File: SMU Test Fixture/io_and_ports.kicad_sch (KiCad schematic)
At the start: 45 parts, among them J1 AD2 Connector, J10 Ext. Source, J11 Conn_01x03, J12 105-1102-001, J2 Scope -1, J3 Scope +1, J4 Scope -2, J5 Scope +2, J6 WG1, J7 WG2, J8 AD2 Connector, J9 105-1102-001, U10 ADGS1412, U11 ADGS1412, U16 OPA189IDBVx, U17 OPA189IDBVx, U8 ADGS1412, U9 ADGS1412

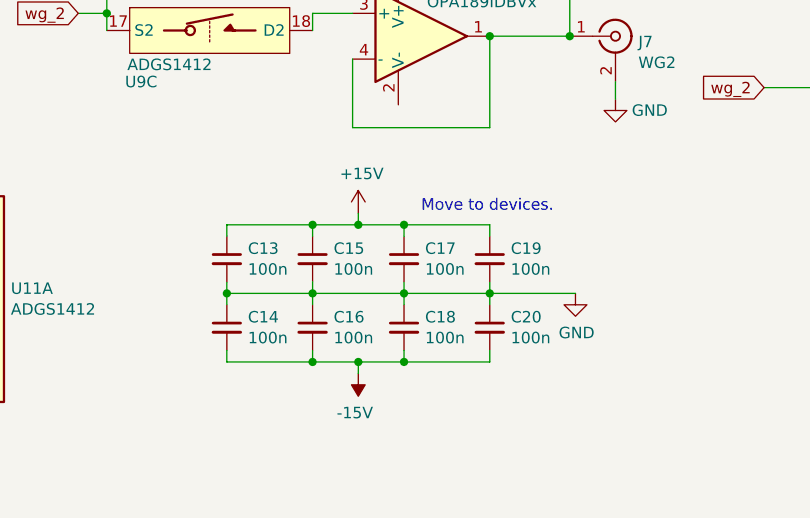
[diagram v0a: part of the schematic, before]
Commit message: Move bypass caps to devices
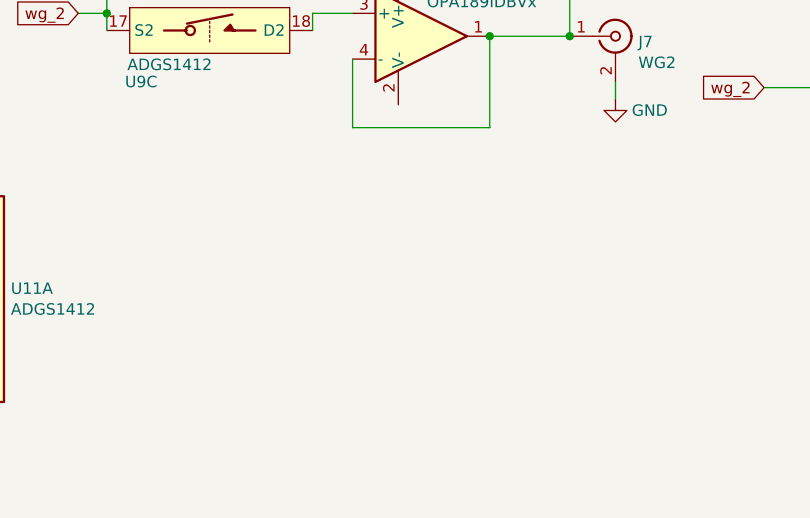
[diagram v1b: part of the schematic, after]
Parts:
- removed C13, C14, C15, C16, C17, C18, C19, C20: 100n, Capacitor_SMD:C_0805_2012Metric_Pad1.18x1.45mm_HandSolder, symbol Device:C_Small
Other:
- note removed: "Move to devices."

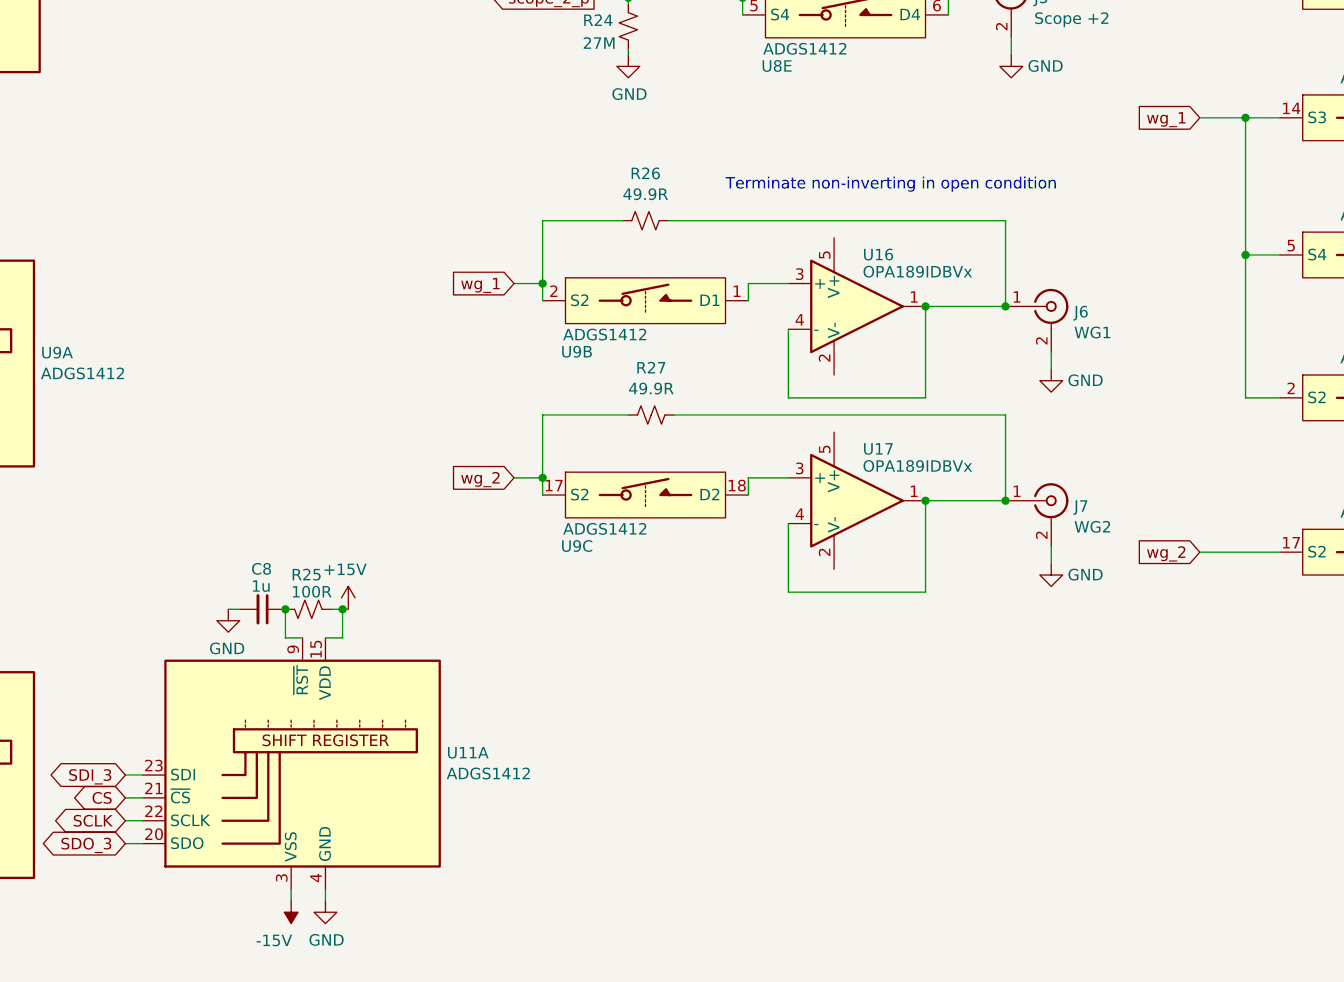
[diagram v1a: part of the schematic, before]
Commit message: Use relay for wavegen output termination.
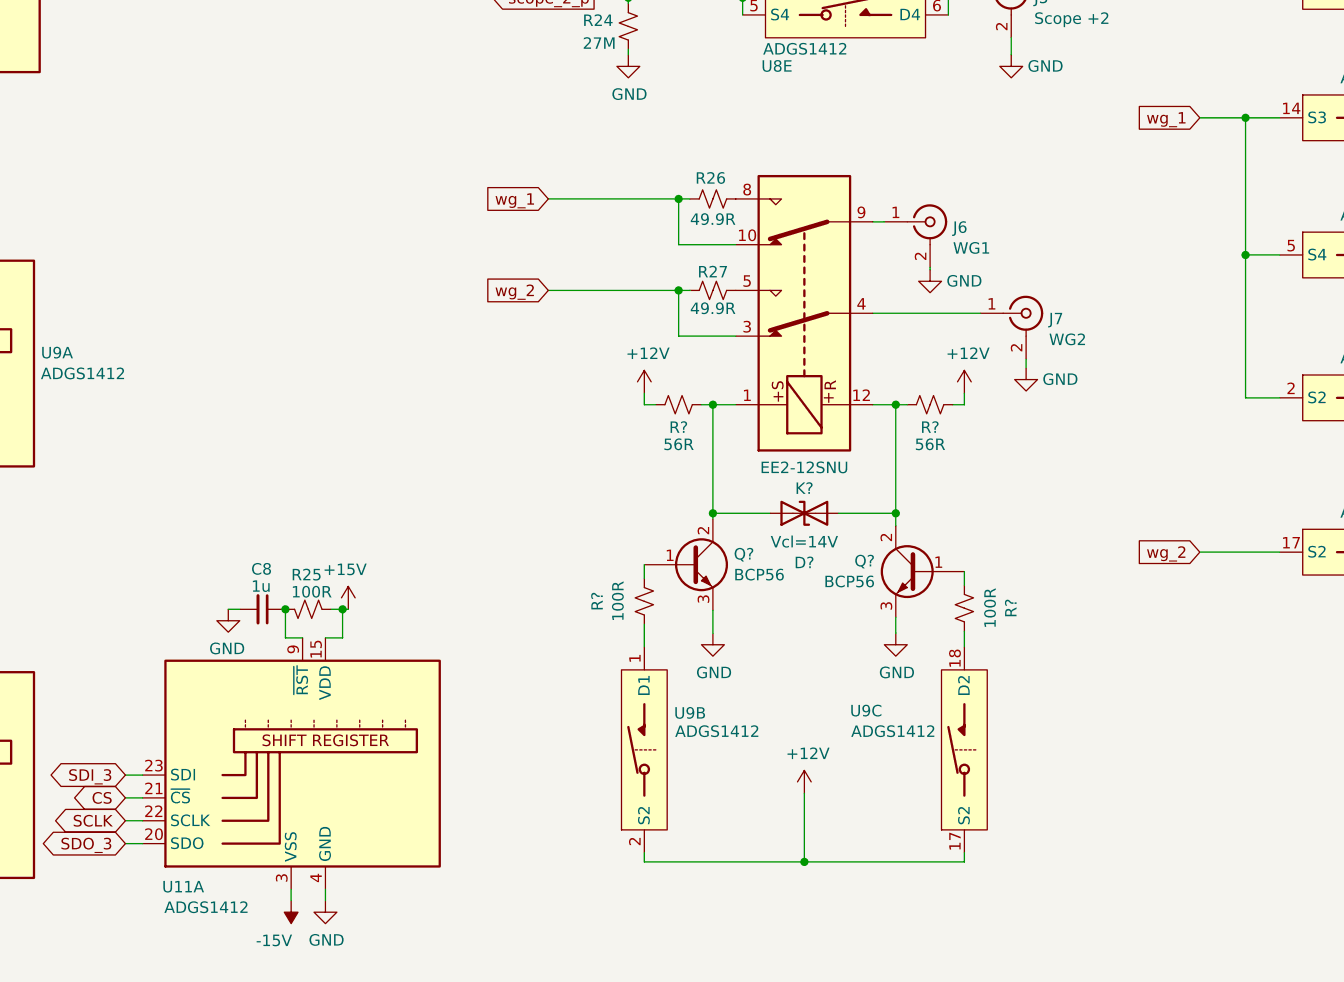
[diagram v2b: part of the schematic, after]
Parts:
- removed U16, U17: OPA189IDBVx, Package_TO_SOT_SMD:SOT-23-5_HandSoldering, symbol SMUTestFixture-rescue:OPA189IDBVx-MAGI_Symbols
- added D?: Vcl=14V, Diode_SMD:D_0201_0603Metric_Pad0.64x0.40mm_HandSolder, symbol Device:D_TVS
- added K?: EE2-12SNU, Relay_SMD:Relay_DPDT_Kemet_EE2_NU, symbol Relay:EE2-12SNU
- added Q? (x2): BCP56, Package_TO_SOT_SMD:SOT-223-3_TabPin2, symbol Transistor_BJT:BCP56
- added R? (x2): 100R, symbol Device:R_Small_US
- added R? (x2): 56R, symbol Device:R_Small_US
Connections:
- net GND: now also Q?.3 (E), Q?.3 (E)
- net wg_1: now also K?.10; no longer U9.2 (S2)
- net wg_2: now also K?.3; no longer U9.17 (S2)
- net at U9.1 (D1): now also R?.2
- net at U9.18 (D2): now also R?.1
- net at R26.1: now also K?.8; no longer J6.1 (In)
- net at R27.1: now also K?.5; no longer J7.1 (In)
- new net: J6.1 (In), K?.9
- new net: J7.1 (In), K?.4
- new net: Q?.1 (B), R?.2
- new net: Q?.1 (B), R?.1
- new net: D?.1 (A1), K?.1, Q?.2 (C), Q?.4 (C), R?.1
- new net: D?.2 (A2), K?.12, Q?.2 (C), Q?.4 (C), R?.2
- new net +12V: R?.1, R?.2, U9.17 (S2), U9.2 (S2)
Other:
- note removed: "Terminate non-inverting in open condition"
- moved on the sheet: J6, J7, R26, R27, U9B, U9C

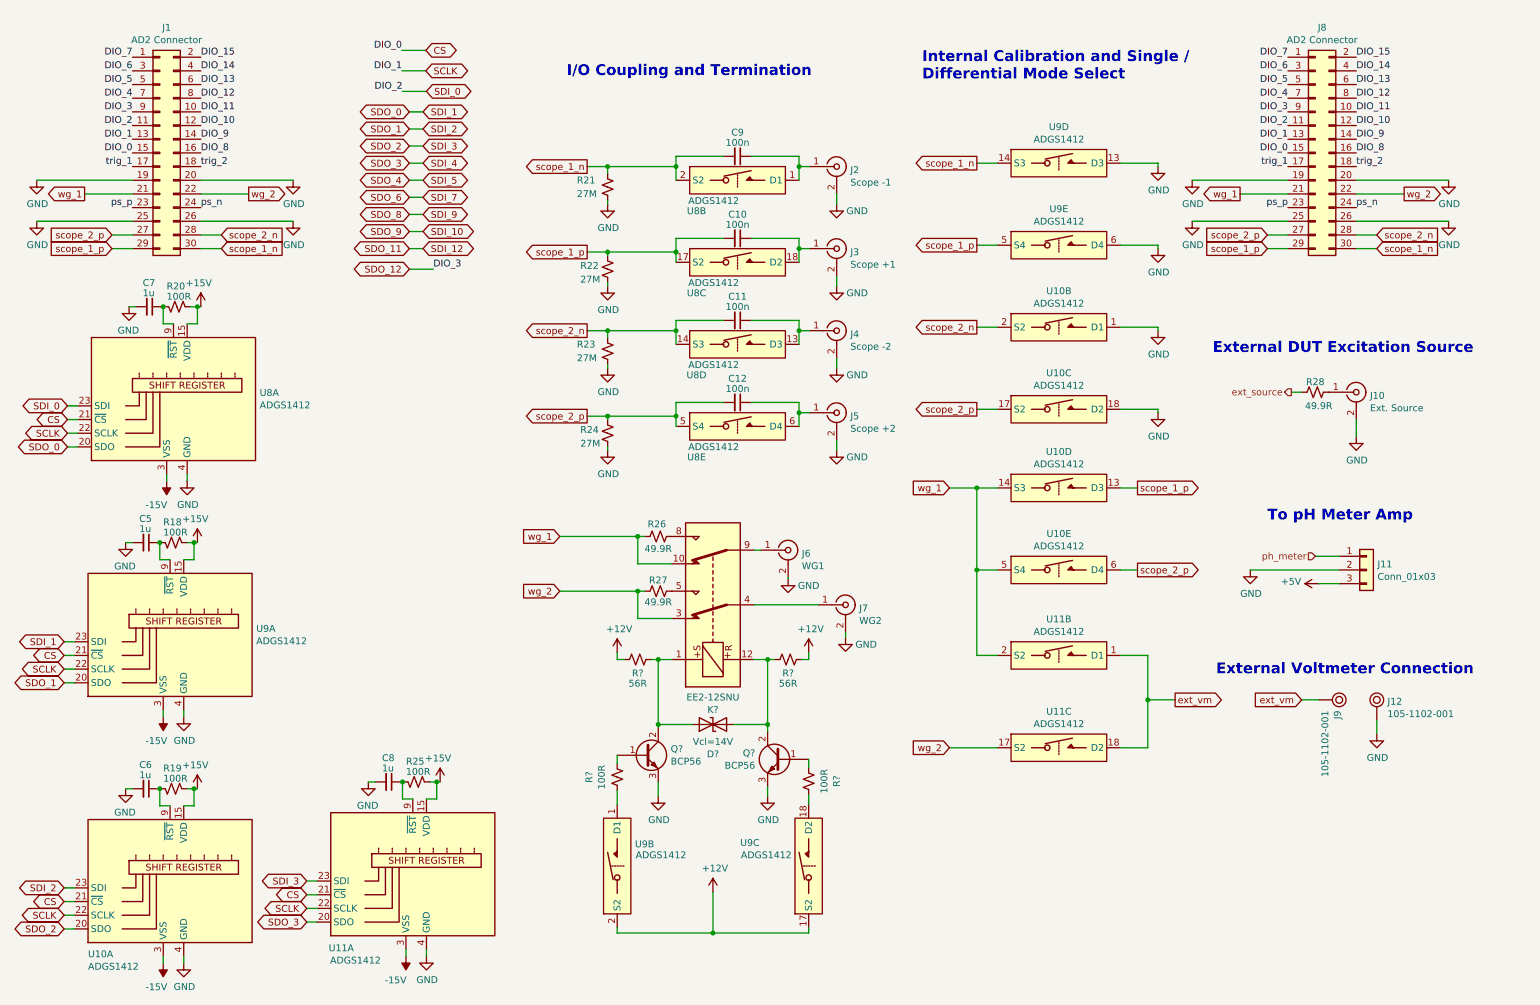
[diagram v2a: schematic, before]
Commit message: Add measurement connections to scope inputs
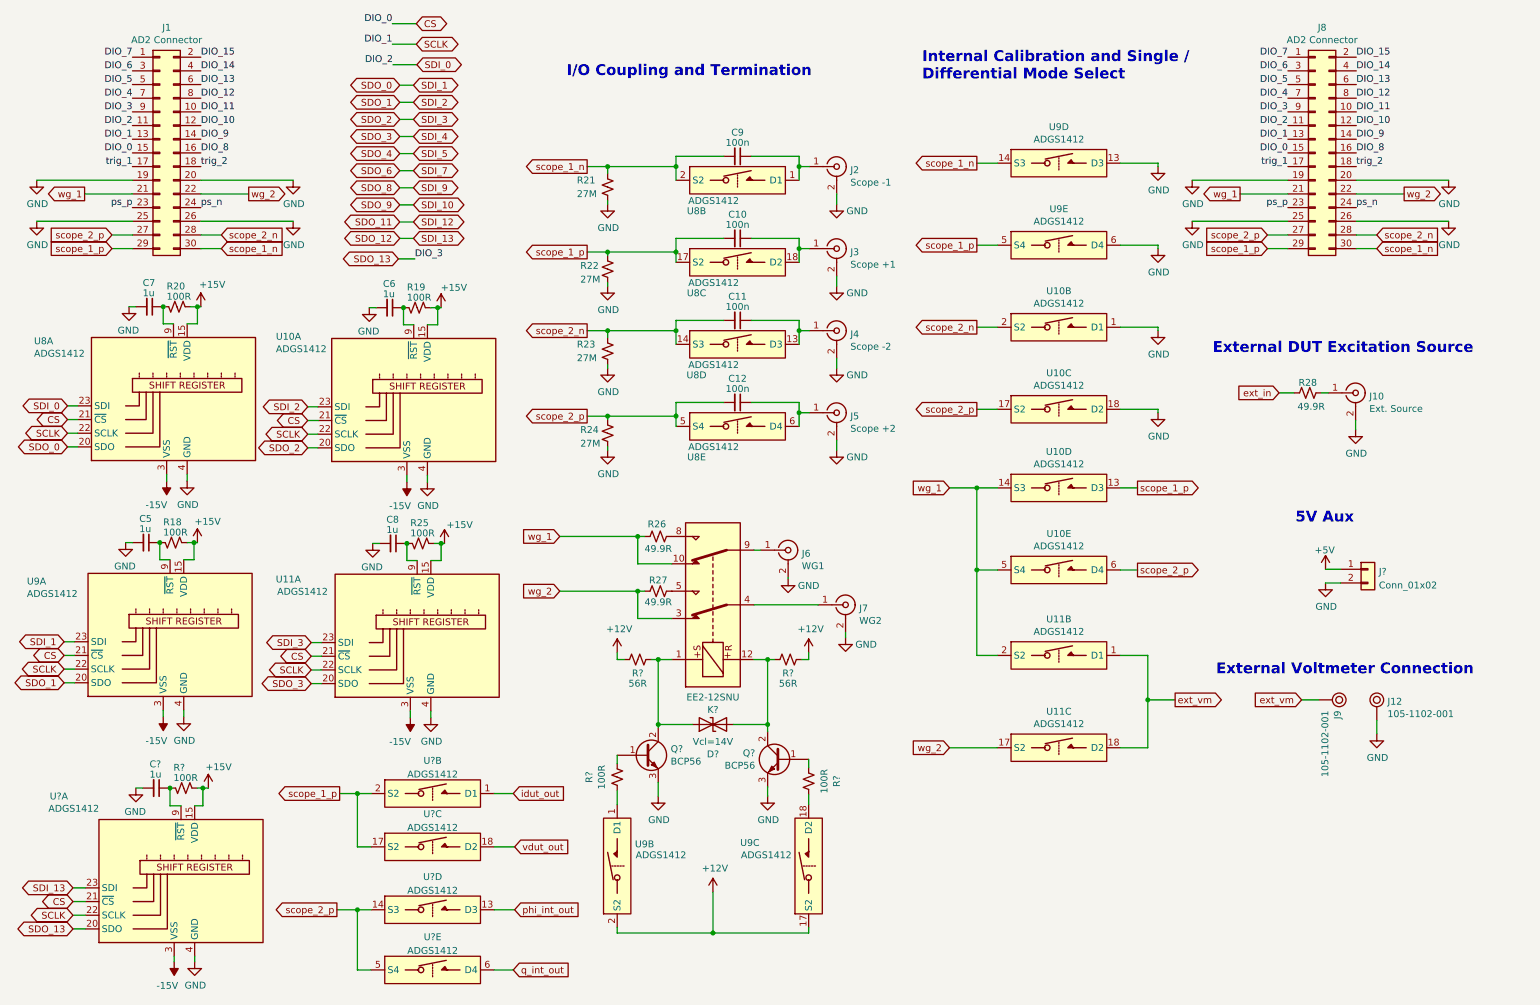
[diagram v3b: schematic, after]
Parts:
- removed J11: Conn_01x03, symbol Connector_Generic:Conn_01x03
- added C?: 1u, symbol Device:C_Small
- added J?: Conn_01x02, symbol Connector_Generic:Conn_01x02
- added R?: 100R, symbol Device:R_Small_US
- added U? (x5): ADGS1412, Package_CSP:LFCSP-24-1EP_4x4mm_P0.5mm_EP2.5x2.5mm, symbol SMUTestFixture-rescue:ADGS1412-MAGI_Symbols
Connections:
- net +15V: now also R?.1, U?.15 (VDD)
- net +5V: now also J?.1 (Pin_1)
- net -15V: now also U?.25 (VSS_PAD), U?.3 (VSS)
- net CS: now also U?.21 (~{CS})
- net GND: now also C?.2, J?.2 (Pin_2), U?.11 (GND), U?.4 (GND)
- net SCLK: now also U?.22 (SCLK)
- net scope_1_p: now also U?.17 (S2), U?.2 (S2)
- net scope_2_p: now also U?.14 (S3), U?.5 (S4)
- net SDO_12 renamed SDO_13
- net SDO_13: now also U?.20 (SDO)
- net ext_source renamed ext_in
- new net: C?.1, R?.2, U?.9 (~{RST})
- new net SDI_13: U?.23 (SDI)
- new net idut_out: U?.1 (D1)
- new net phi_int_out: U?.13 (D3)
- new net q_int_out: U?.6 (D4)
- new net vdut_out: U?.18 (D2)
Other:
- note added: "5V Aux"
- note removed: "To pH Meter Amp"
- moved on the sheet: C6, C8, R19, R25, R28, U10A, U11A

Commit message: Fix grid nightmare. Begin adding bypass caps for a.switches
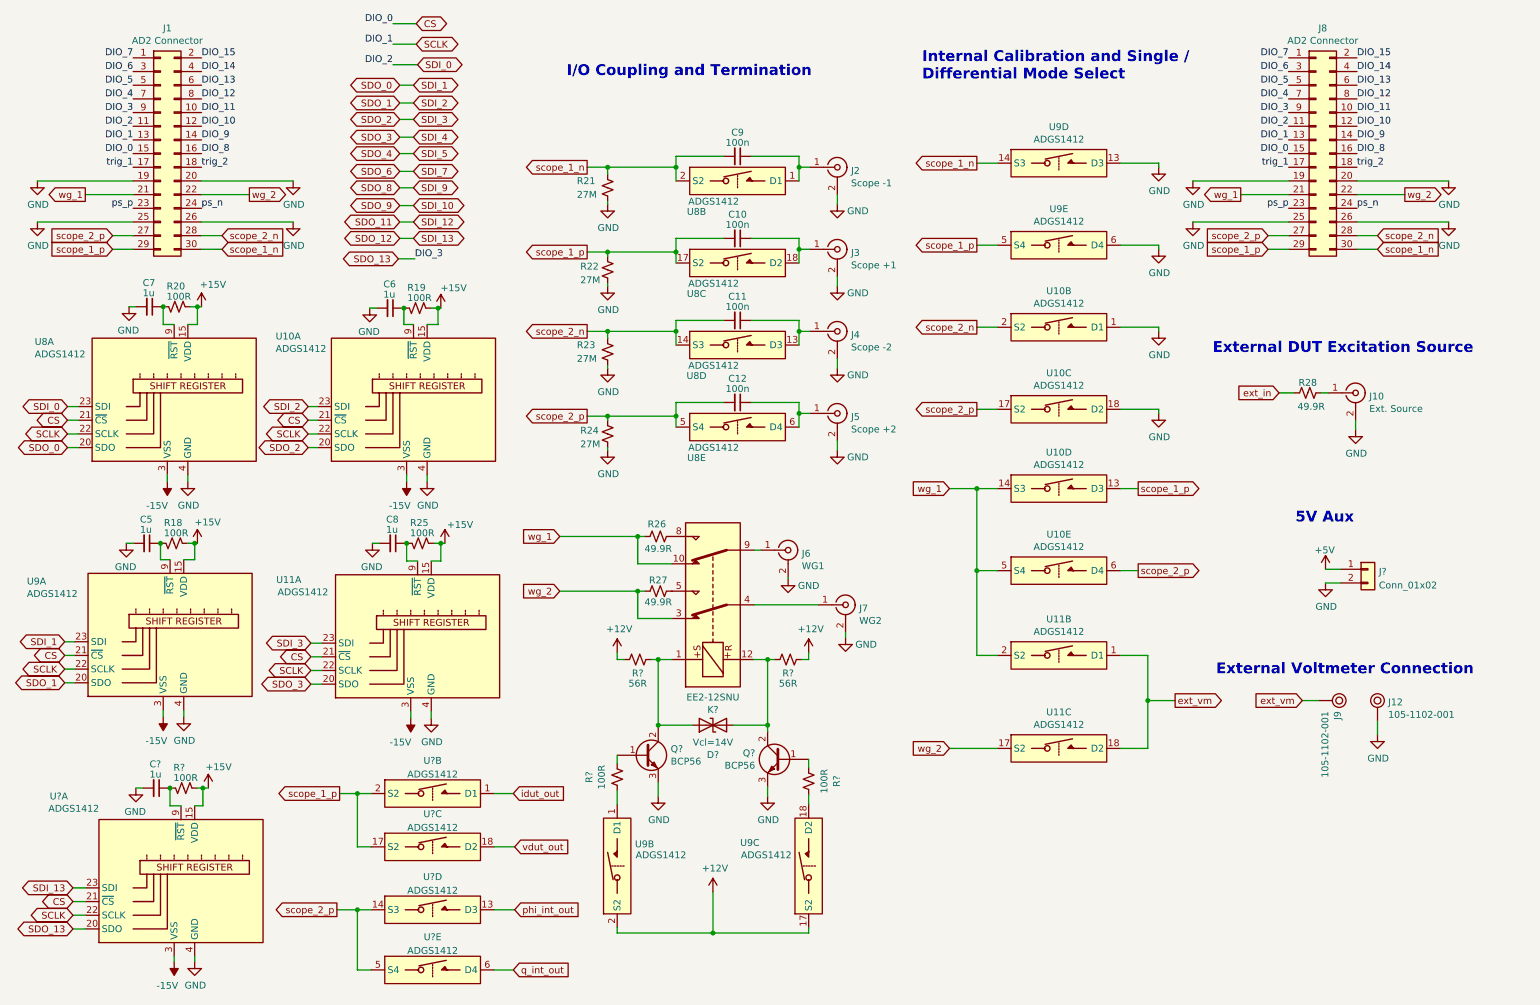
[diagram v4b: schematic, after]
